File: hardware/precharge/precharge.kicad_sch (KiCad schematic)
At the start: 16 parts

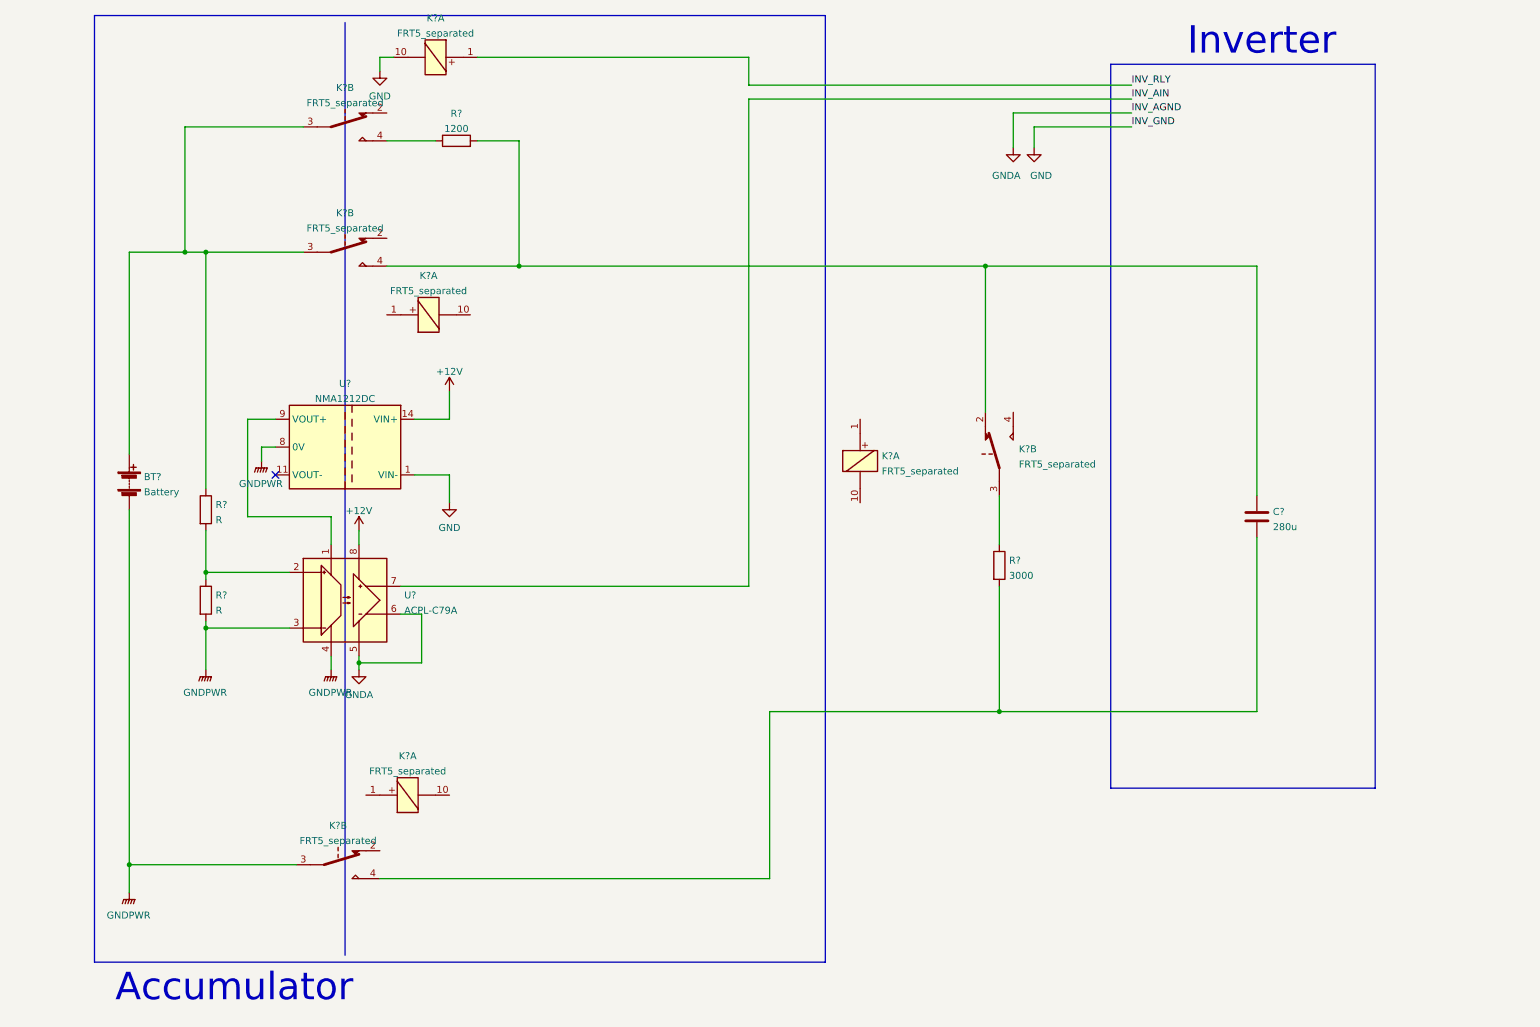
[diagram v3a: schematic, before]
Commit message: Moved outline into a separate directory and created precharge project with just precharge circuitry
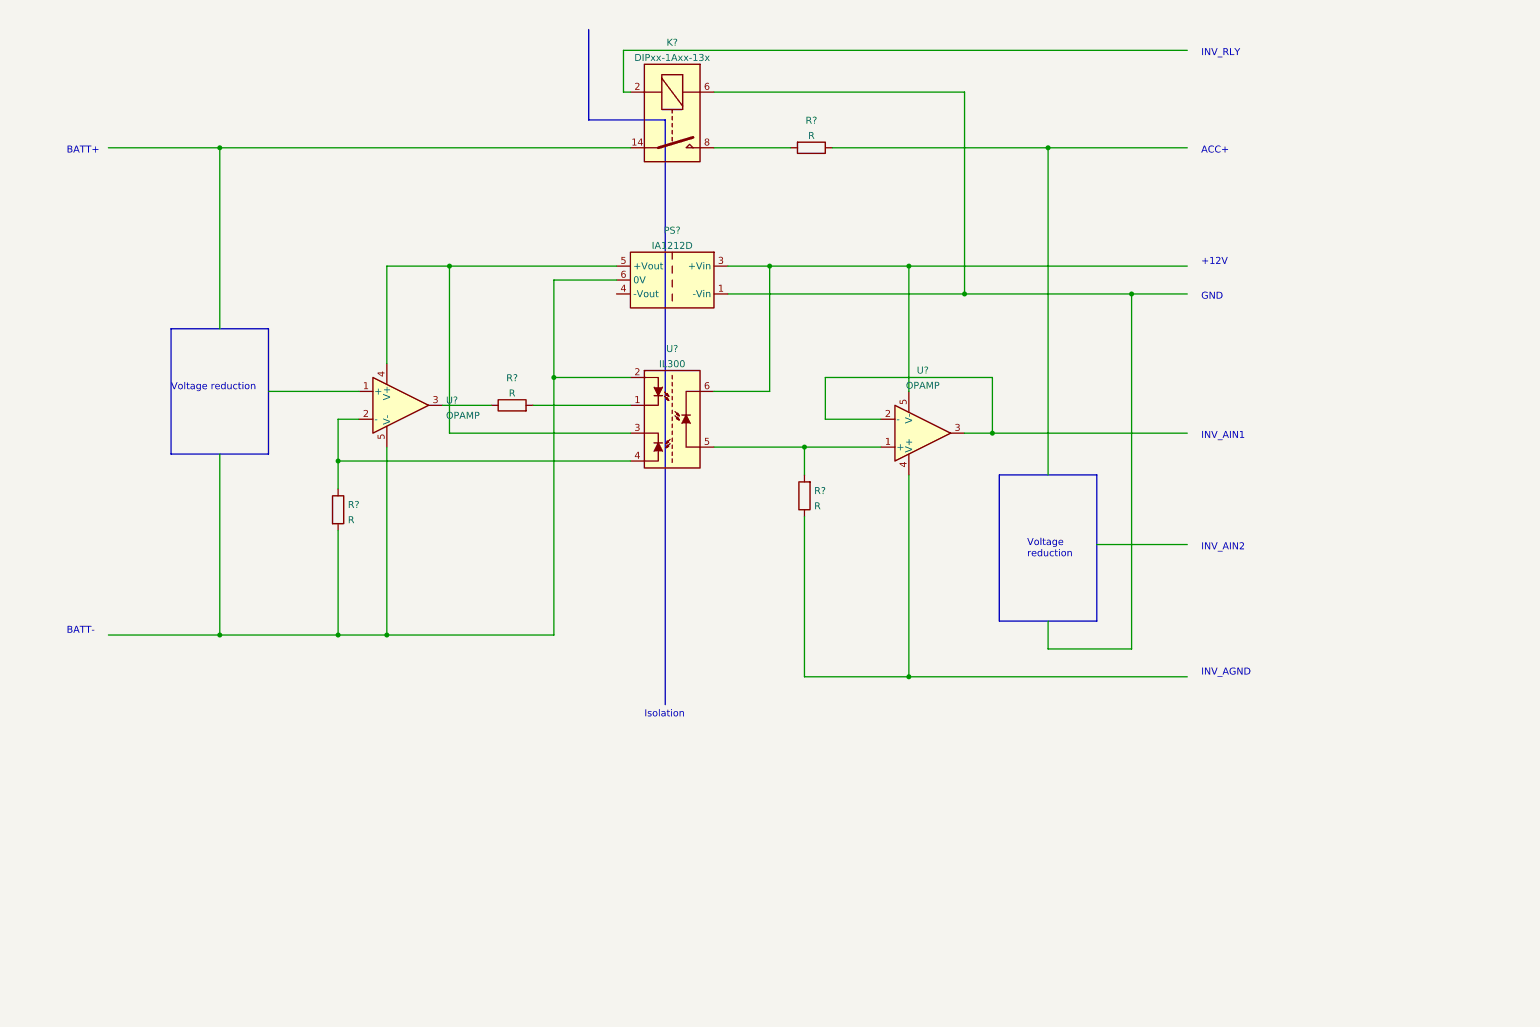
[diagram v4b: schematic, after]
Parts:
- removed BT?: Battery, symbol Device:Battery
- removed C?: 280u, symbol Device:C
- removed K? (x8): FRT5_separated, Relay_THT:Relay_DPDT_FRT5, symbol Relay:FRT5_separated
- removed R? (x2): R, symbol Device:R
- removed R?: 1200, symbol Device:R
- removed R?: 3000, symbol Device:R
- removed U?: NMA1212DC, Converter_DCDC:Converter_DCDC_muRata_NMAxxxxDC_THT, symbol Regulator_Switching:NMA1212DC
- removed U?: ACPL-C79A, Package_SO:SSO-8_6.8x5.9mm_P1.27mm_Clearance8mm, symbol Isolator_Analog:ACPL-C79A
- added K?: DIPxx-1Axx-13x, Relay_THT:Relay_StandexMeder_DIP_LowProfile, symbol Relay:DIPxx-1Axx-13x
- added PS?: IA1212D, Converter_DCDC:Converter_DCDC_XP_POWER-IAxxxxD_THT, symbol Converter_DCDC:IA1212D
- added R? (x4): R, symbol Device:R
- added U?: IL300, symbol Isolator_Analog:IL300
- added U? (x2): OPAMP, symbol Simulation_SPICE:OPAMP
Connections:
- new net: K?.8, R?.2
- new net: K?.6, PS?.1 (-Vin)
- new net: R?.1, U?.3
- new net: R?.2, U?.1
- new net: PS?.6 (0V), R?.2, U?.2, U?.5 (V-)
- new net: PS?.5 (+Vout), U?.3, U?.4 (V+)
- new net: R?.1, U?.2 (-), U?.4
- new net: R?.2, U?.1 (+), U?.5
- new net: PS?.3 (+Vin), U?.5 (V-), U?.6
- new net: R?.1, U?.4 (V+)
- new net: U?.2 (-), U?.3
- no-connect marks 1 -> 0
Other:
- note added: "+12V"
- note added: "ACC+"
- note added: "BATT+"
- note added: "BATT-"
- note added: "GND"
- note added: "INV_AGND"
- note added: "INV_AIN1"
- note added: "INV_AIN2"
- note added: "INV_RLY"
- note added: "Isolation"
- note added: "Voltage reduction"
- note removed: "Accumulator"
- note removed: "Inverter"

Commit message: Misc. changes to schematic, created PCB
The PCB was created just to begin modelling its size.
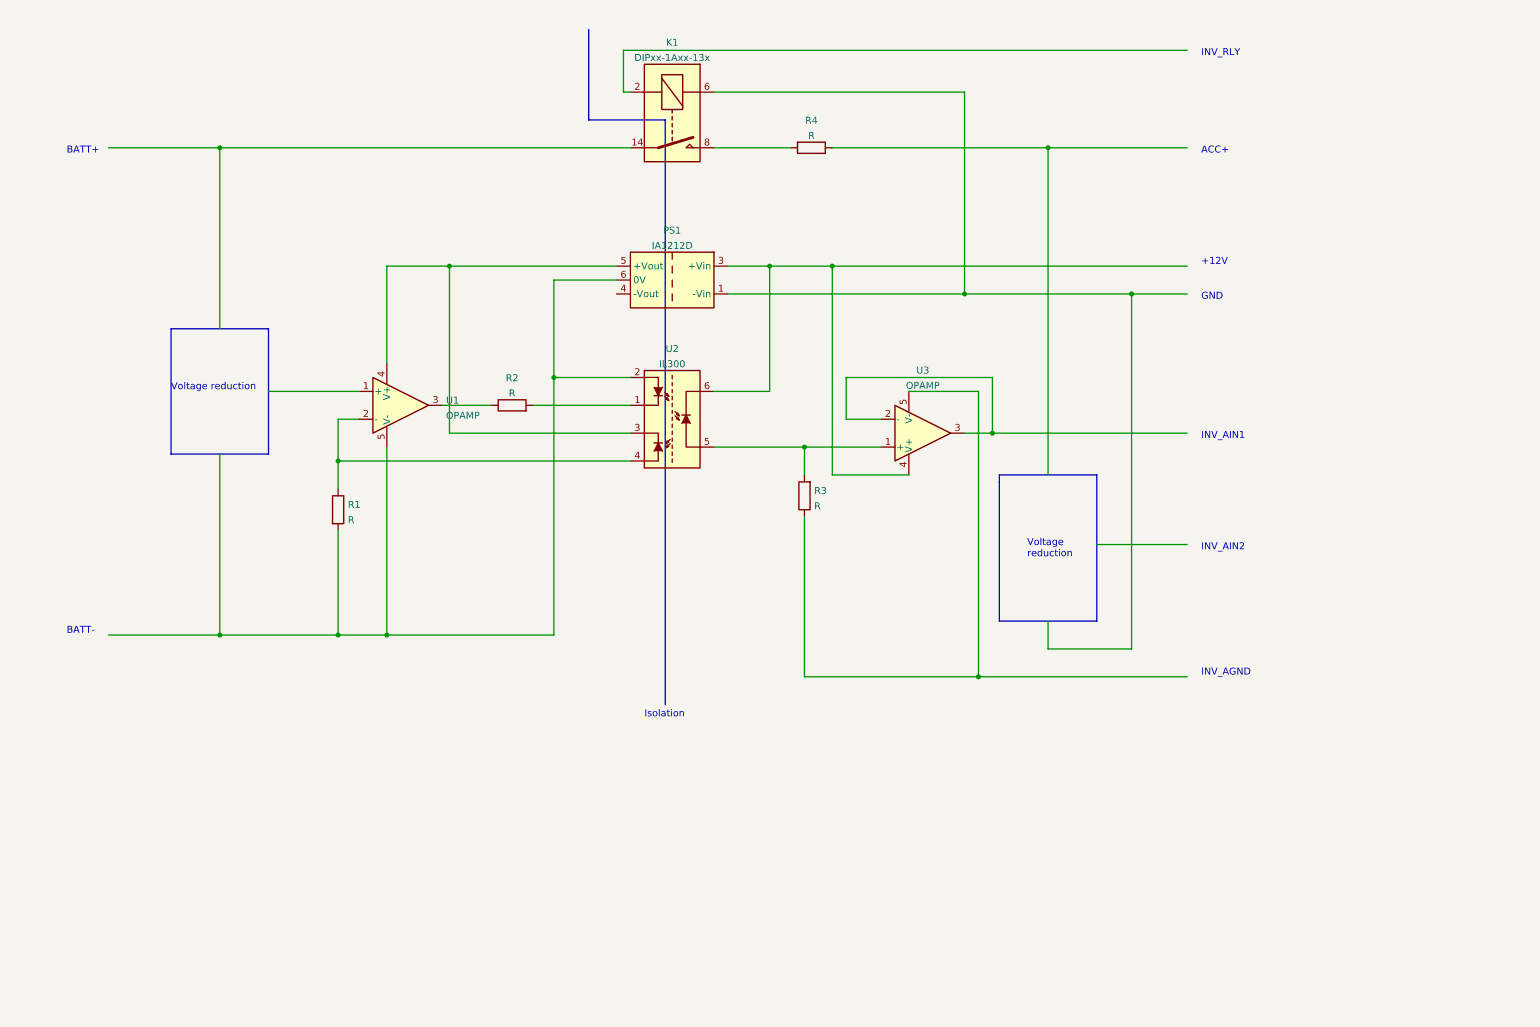
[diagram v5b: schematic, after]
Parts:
- U1, U3: renamed from U?; footprint (none) -> Package_TO_SOT_SMD:SOT-23-5
- U2: renamed from U?; footprint (none) -> Package_DIP:DIP-8_W7.62mm
- gave numbers to parts that had none: 6
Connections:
- net at PS1.3 (+Vin), U2.6: now also U3.4 (V+); no longer U3.5 (V-)
- net at R3.1: now also U3.5 (V-); no longer U3.4 (V+)

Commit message: Major changes to schematic
- Split into HV and LV sections

- Implemented most of the precharge logic
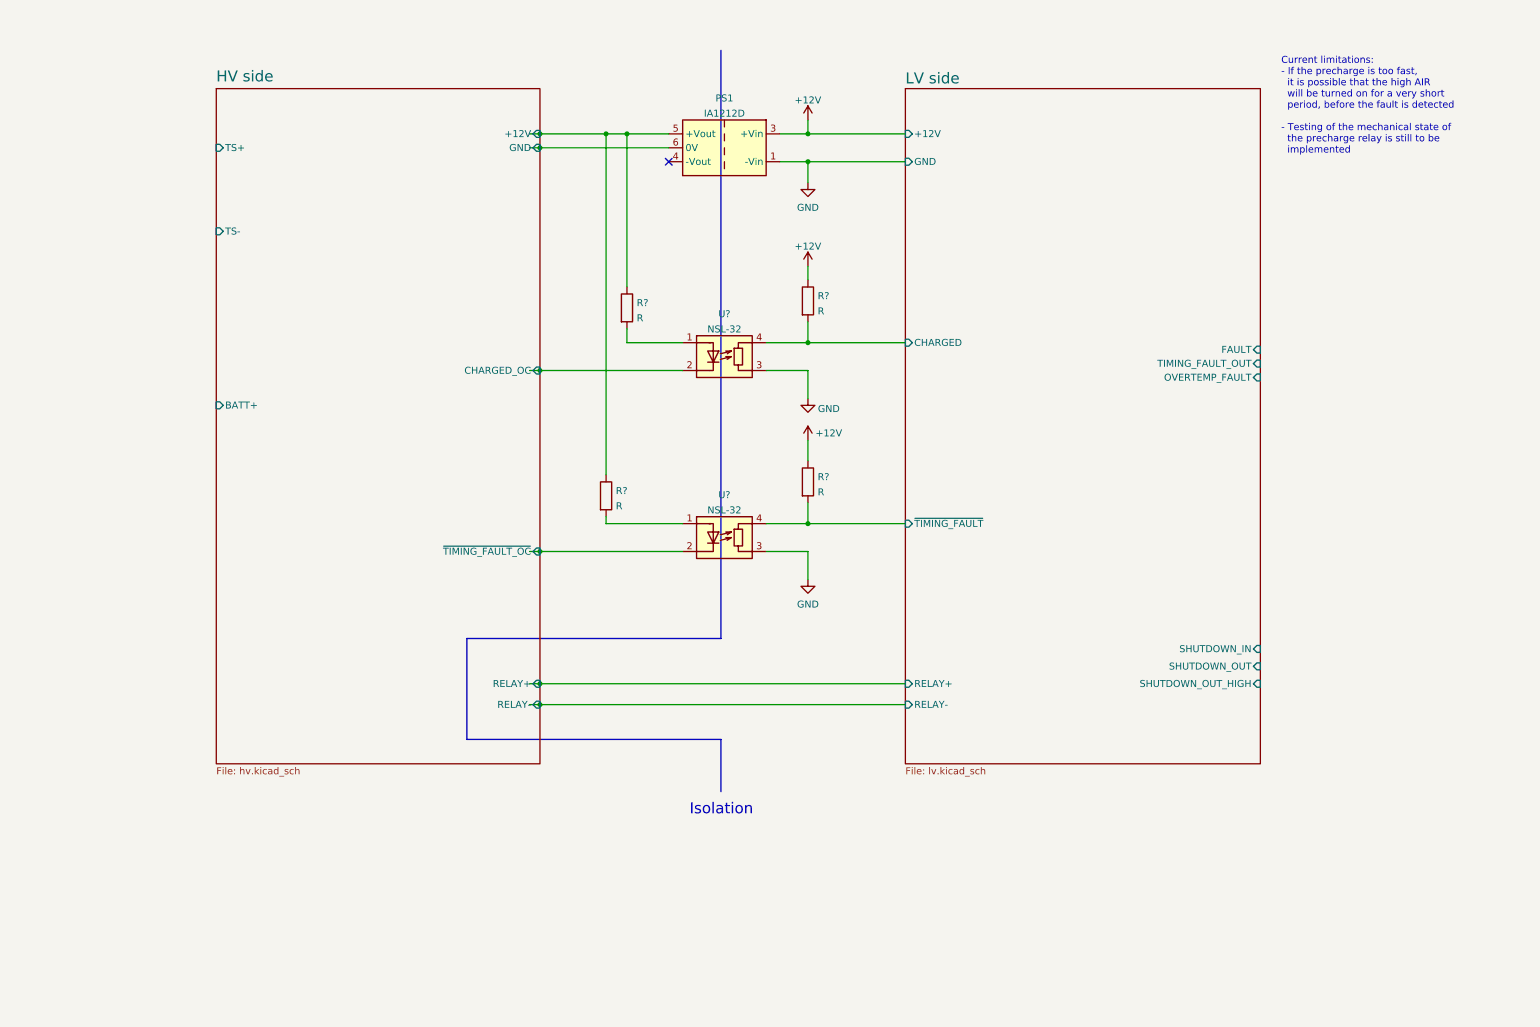
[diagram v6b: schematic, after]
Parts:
- removed K1: DIPxx-1Axx-13x, Relay_THT:Relay_StandexMeder_DIP_LowProfile, symbol Relay:DIPxx-1Axx-13x
- removed R1, R2, R3, R4: R, symbol Device:R
- removed U1, U3: OPAMP, Package_TO_SOT_SMD:SOT-23-5, symbol Simulation_SPICE:OPAMP
- removed U2: IL300, Package_DIP:DIP-8_W7.62mm, symbol Isolator_Analog:IL300
- added R? (x4): R, symbol Device:R
- added U? (x2): NSL-32, OptoDevice:Luna_NSL-32, symbol Isolator:NSL-32
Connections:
- net GND: now reaches PS1.1 (-Vin)
- net GND: now also U?.3 (R), U?.3 (R)
- net HV side/GND: now reaches PS1.6 (0V)
- net HV side/+12V: now reaches PS1.5 (+Vout)
- net HV side/+12V: now also R?.1, R?.1
- net +12V: now reaches PS1.3 (+Vin)
- net +12V: now also R?.1, R?.1
- new net: R?.2, U?.1 (A) (x2)
- new net HV side/CHARGED_OC: U?.2 (K)
- new net HV side/~{TIMING_FAULT_OC}: U?.2 (K)
- new net LV side/CHARGED: R?.2, U?.4 (R)
- new net LV side/~{TIMING_FAULT}: R?.2, U?.4 (R)
- no-connect marks 0 -> 1
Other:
- added sheet HV side (hv.kicad_sch)
- added sheet LV side (lv.kicad_sch)
- note added: "Current limitations: - If the precharge is too fast, it is possible that the high AIR will be turned on for a very short period, before the fault is detected - Testing of the mechanical state of the precharge relay is still to be implemented"
- note removed: "+12V"
- note removed: "ACC+"
- note removed: "BATT+"
- note removed: "BATT-"
- note removed: "GND"
- note removed: "INV_AGND"
- note removed: "INV_AIN1"
- note removed: "INV_AIN2"
- note removed: "INV_RLY"
- note removed: "Voltage reduction"
- moved on the sheet: PS1

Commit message: Tweaks made during today's meeting
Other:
- note added: "Current limitations: - If the precharge is too fast, it is possible that the high AIR will be turned on for a very short period, before the fault is detected - Testing of the mechanical state of the precharge relay is still to be implemented - The 12V must be turned on before the shutdown circuit is closed (with enough time for the systems to initialise)"
- note removed: "Current limitations: - If the precharge is too fast, it is possible that the high AIR will be turned on for a very short period, before the fault is detected - Testing of the mechanical state of the precharge relay is still to be implemented"
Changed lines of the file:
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@@
     (effects (font (size 2 2)) (justify left bottom))
   )
-  (text "Current limitations:\n- If the precharge is too fast,\n  it is possible that the high AIR\n  will be turned on for a very short\n  period, before the fault is detected\n\n- Testing of the mechanical state of\n  the precharge relay is still to be\n  implemented"
-    (at 245.745 39.37 0)
+  (text "Current limitations:\n- If the precharge is too fast,\n  it is possible that the high AIR\n  will be turned on for a very short\n  period, before the fault is detected\n\n- Testing of the mechanical state of\n  the precharge relay is still to be\n  implemented\n\n- The 12V must be turned on before\n  the shutdown circuit is closed\n  (with enough time for the systems\n  to initialise)"
+    (at 245.11 50.8 0)
     (effects (font (size 1.27 1.27)) (justify left bottom))
   )
@@
       (reference "R?") (unit 1) (value "R") (footprint "")
     )
+    (path "/86ebb052-21e6-4e49-945d-049a70338ab6/15dfdd0f-8f86-48e1-bef4-033654d9612f"
+      (reference "R?") (unit 1) (value "R") (footprint "")
+    )
     (path "/17b21d20-64c8-472f-8c8f-00c20b37266b"
       (reference "R?") (unit 1) (value "R") (footprint "")
@@
       (reference "U?") (unit 4) (value "40106") (footprint "")
     )
+    (path "/86ebb052-21e6-4e49-945d-049a70338ab6/741ade0e-280d-4ca1-95c1-c006eda937d0"
+      (reference "U?") (unit 4) (value "LM339") (footprint "")
+    )
     (path "/a25b3faf-d95a-49ad-9b40-7c3f8d869233/3257ca68-ab5f-4c77-a85e-9fb6ecad8b0d"
